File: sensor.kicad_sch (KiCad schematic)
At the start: 6 parts

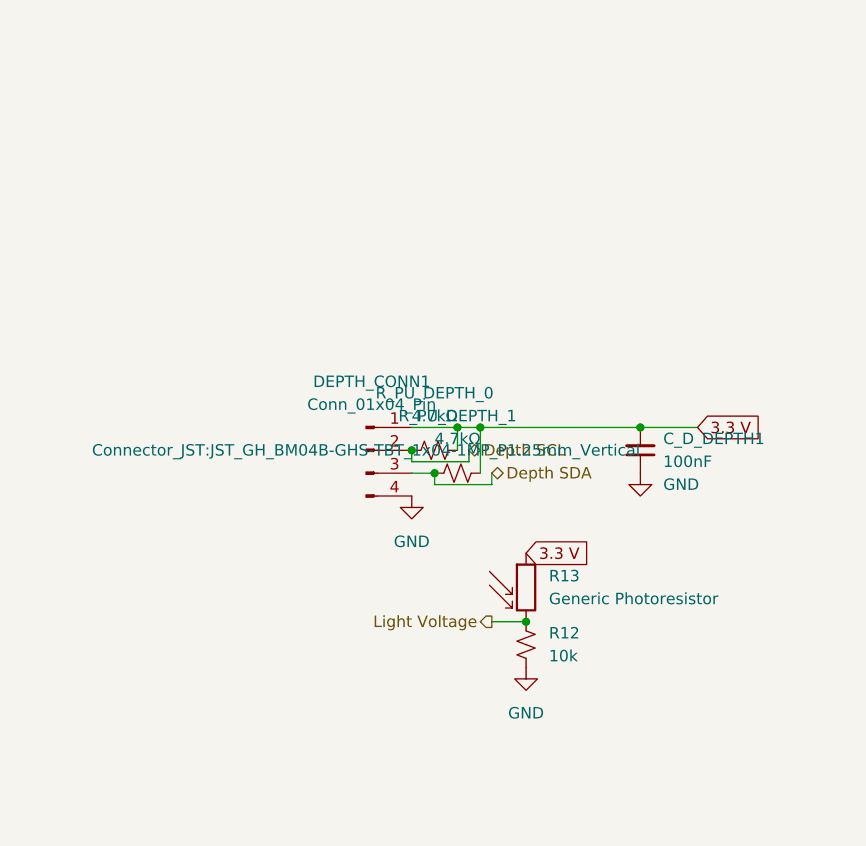
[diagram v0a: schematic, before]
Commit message: Updated Schematic
Updated schematic
Cleaned up dense portions
added H bridge
correct i2c wiring
added ferrite beads
added 12 V power monitoring
added stlink
added power mux
added power from usb
reformatted hierarichal sheets
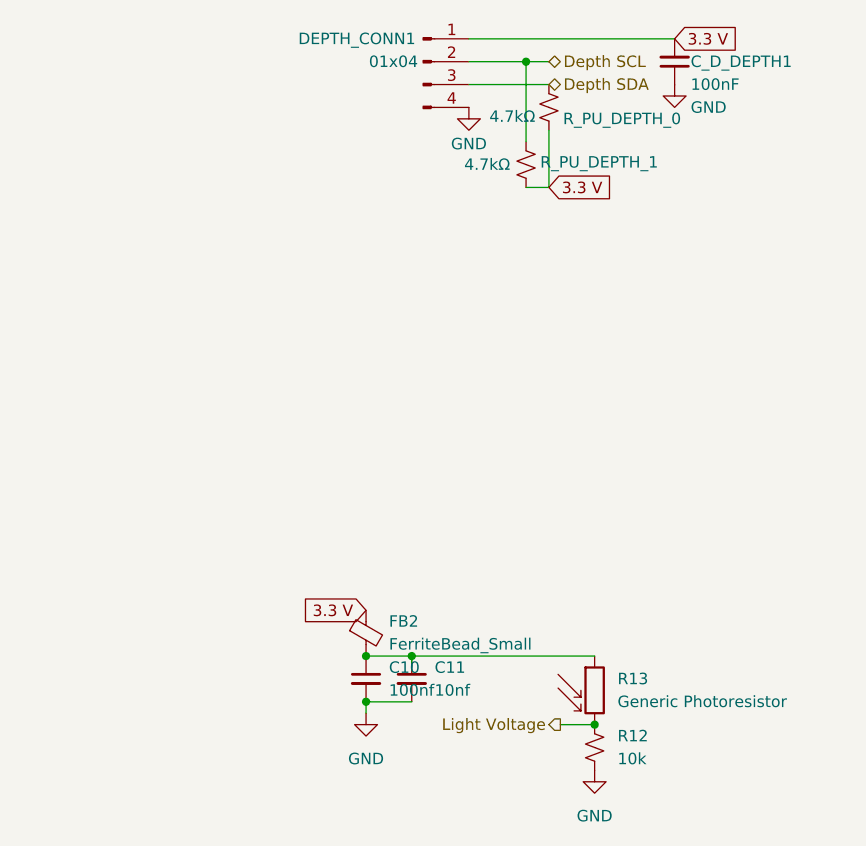
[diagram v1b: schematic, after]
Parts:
- added C10: 100nf, symbol Device:C_Small
- added C11: 10nf, symbol Device:C_Small
- added FB2: FerriteBead_Small, symbol Device:FerriteBead_Small
- DEPTH_CONN1: value Conn_01x04_Pin -> 01x04
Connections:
- net 3.3 V: now also R_PU_DEPTH_1.1, FB2.1; no longer R13.1, R_PU_DEPTH_1.2
- net Depth SCL: now also R_PU_DEPTH_1.2; no longer R_PU_DEPTH_0.1
- net Depth SDA: now also R_PU_DEPTH_0.1; no longer R_PU_DEPTH_1.1
- net GND: now also C10.2, C11.2
- new net: C10.1, C11.1, FB2.2, R13.1
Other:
- moved on the sheet: C_D_DEPTH1, DEPTH_CONN1, R12, R13, R_PU_DEPTH_0, R_PU_DEPTH_1

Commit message: USB, TVS, LDO, Passives, I2C
applied changes to usb circuitry, tvs, ldo, passibes and i2c.
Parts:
- removed R_PU_DEPTH_0, R_PU_DEPTH_1: 4.7kΩ, Resistor_SMD:R_0603_1608Metric, symbol Device:R_Small_US
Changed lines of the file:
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@@
-	)
-	(junction
-		(at 43.18 22.86)
-		(diameter 0)
-		(color 0 0 0 0)
 	)
 	(junction
@@
 	(wire
 		(pts
-			(xy 43.18 22.86) (xy 45.72 22.86)
+			(xy 36.83 22.86) (xy 45.72 22.86)
 		)
 		(stroke
@@
 	(wire
 		(pts
-			(xy 45.72 30.48) (xy 45.72 36.83)
+			(xy 50.8 88.9) (xy 30.48 88.9)
 		)
 		(stroke
@@
 	(wire
 		(pts
-			(xy 43.18 36.83) (xy 45.72 36.83)
+			(xy 36.83 25.4) (xy 45.72 25.4)
 		)
 		(stroke
@@
 	(wire
 		(pts
-			(xy 50.8 88.9) (xy 30.48 88.9)
+			(xy 25.4 93.98) (xy 25.4 95.25)
 		)
 		(stroke
@@
 	(wire
 		(pts
-			(xy 36.83 25.4) (xy 45.72 25.4)
-		)
-		(stroke
-			(width 0)
-			(type default)
-		)
-	)
-	(wire
-		(pts
-			(xy 25.4 93.98) (xy 25.4 95.25)
-		)
-		(stroke
-			(width 0)
-			(type default)
-		)
-	)
-	(wire
-		(pts
-			(xy 36.83 22.86) (xy 43.18 22.86)
-		)
-		(stroke
-			(width 0)
-			(type default)
-		)
-	)
-	(wire
-		(pts
 			(xy 25.4 93.98) (xy 30.48 93.98)
-		)
-		(stroke
-			(width 0)
-			(type default)
-		)
-	)
-	(wire
-		(pts
-			(xy 43.18 22.86) (xy 43.18 31.75)
 		)
 		(stroke
@@
 				)
 				(justify right)
-			)
-		)
-	)
-	(global_label "3.3 V"
-		(shape input)
-		(at 45.72 36.83 0)
-		(fields_autoplaced yes)
-		(effects
-			(font
-				(size 1.27 1.27)
-			)
-			(justify left)
-		)
-		(property "Intersheetrefs" "${INTERSHEET_REFS}"
-			(at 53.7852 36.83 0)
-			(hide yes)
-			(show_name no)
-			(do_not_autoplace no)
-			(effects
-				(font
-					(size 1.27 1.27)
-				)
-				(justify left)
 			)
 		)
@@
 	)
 	(symbol
-		(lib_id "Device:R_Small_US")
-		(at 43.18 34.29 180)
-		(unit 1)
-		(body_style 1)
-		(exclude_from_sim no)
-		(in_bom yes)
-		(on_board yes)
-		(in_pos_files yes)
-		(dnp no)
-		(property "Reference" "R_PU_DEPTH_1"
-			(at 51.308 34.036 0)
-			(show_name no)
-			(do_not_autoplace no)
-			(effects
-				(font
-					(size 1.27 1.27)
-				)
-			)
-		)
-		(property "Value" "4.7kΩ"
-			(at 38.862 34.29 0)
-			(show_name no)
-			(do_not_autoplace no)
-			(effects
-				(font
-					(size 1.27 1.27)
-				)
-			)
-		)
-		(property "Footprint" "Resistor_SMD:R_0603_1608Metric"
-			(at 43.18 34.29 0)
-			(hide yes)
-			(show_name no)
-			(do_not_autoplace no)
-			(effects
-				(font
-					(size 1.27 1.27)
-				)
-			)
-		)
-		(property "Datasheet" ""
-			(at 43.18 34.29 0)
-			(hide yes)
-			(show_name no)
-			(do_not_autoplace no)
-			(effects
-				(font
-					(size 1.27 1.27)
-				)
-			)
-		)
-		(property "Description" "Resistor, small US symbol"
-			(at 43.18 34.29 0)
-			(hide yes)
-			(show_name no)
-			(do_not_autoplace no)
-			(effects
-				(font
-					(size 1.27 1.27)
-				)
-			)
-		)
-		(pin "1"
-		)
-		(pin "2"
-		)
-		(instances
-			(project "X19-Float-Board"
-				(path "/00000000-0000-0000-0000-000060e6118b/5f356ab3-657b-42f3-9a8b-ebc79580ebf5"
-					(reference "R_PU_DEPTH_1")
-					(unit 1)
-				)
-			)
-		)
-	)
-	(symbol
 		(lib_id "Connector:Conn_01x04_Pin")
 		(at 31.75 22.86 0)
@@
 					(unit 1)
 				)
-			)
-		)
-	)
-	(symbol
-		(lib_id "Device:R_Small_US")
-		(at 45.72 27.94 0)
-		(unit 1)
-		(body_style 1)
-		(exclude_from_sim no)
-		(in_bom yes)
-		(on_board yes)
-		(in_pos_files yes)
-		(dnp no)
-		(property "Reference" "R_PU_DEPTH_0"
-			(at 53.848 29.21 0)
-			(show_name no)
-			(do_not_autoplace no)
-			(effects
-				(font
-					(size 1.27 1.27)
-				)
-			)
-		)
-		(property "Value" "4.7kΩ"
-			(at 41.656 28.956 0)
-			(show_name no)
-			(do_not_autoplace no)
-			(effects
-				(font
-					(size 1.27 1.27)
-				)
-			)
-		)
-		(property "Footprint" "Resistor_SMD:R_0603_1608Metric"
-			(at 45.72 27.94 0)
-			(hide yes)
-			(show_name no)
-			(do_not_autoplace no)
-			(effects
-				(font
-					(size 1.27 1.27)
-				)
-			)
-		)
-		(property "Datasheet" ""
-			(at 45.72 27.94 0)
-			(hide yes)
-			(show_name no)
-			(do_not_autoplace no)
-			(effects
-				(font
-					(size 1.27 1.27)
-				)
-			)
-		)
-		(property "Description" "Resistor, small US symbol"
-			(at 45.72 27.94 0)
-			(hide yes)
-			(show_name no)
-			(do_not_autoplace no)
-			(effects
-				(font
-					(size 1.27 1.27)
-				)
-			)
-		)
-		(pin "1"
-		)
-		(pin "2"
-		)
-		(instances
-			(project "X19-Float-Board"
-				(path "/00000000-0000-0000-0000-000060e6118b/5f356ab3-657b-42f3-9a8b-ebc79580ebf5"
-					(reference "R_PU_DEPTH_0")
-					(unit 1)
-				)

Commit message: footprints
footprints
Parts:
- removed FB2: FerriteBead_Small, symbol Device:FerriteBead_Small
- C10, C11: footprint (none) -> Capacitor_SMD:C_0603_1608Metric_Pad1.08x0.95mm_HandSolder
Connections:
- net 3.3 V: now also C10.1, C11.1, R13.1
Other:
- moved on the sheet: C10, C11
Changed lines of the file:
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@@
 	(paper "A4")
 	(junction
-		(at 25.4 88.9)
+		(at 30.48 85.09)
 		(diameter 0)
 		(color 0 0 0 0)
 	)
 	(junction
-		(at 30.48 88.9)
+		(at 25.4 85.09)
+		(diameter 0)
+		(color 0 0 0 0)
+	)
+	(junction
+		(at 50.8 96.52)
 		(diameter 0)
 		(color 0 0 0 0)
@@
 		(color 0 0 0 0)
 	)
-	(junction
-		(at 50.8 96.52)
-		(diameter 0)
-		(color 0 0 0 0)
-	)
 	(wire
 		(pts
@@
 	(wire
 		(pts
-			(xy 30.48 88.9) (xy 30.48 90.17)
-		)
-		(stroke
-			(width 0)
-			(type default)
-		)
-	)
-	(wire
-		(pts
-			(xy 25.4 88.9) (xy 30.48 88.9)
+			(xy 25.4 85.09) (xy 30.48 85.09)
 		)
 		(stroke
@@
 	(wire
 		(pts
-			(xy 50.8 88.9) (xy 30.48 88.9)
+			(xy 25.4 93.98) (xy 25.4 95.25)
+		)
+		(stroke
+			(width 0)
+			(type default)
+		)
+	)
+	(wire
+		(pts
+			(xy 50.8 85.09) (xy 30.48 85.09)
+		)
+		(stroke
+			(width 0)
+			(type default)
+		)
+	)
+	(wire
+		(pts
+			(xy 30.48 85.09) (xy 30.48 87.63)
 		)
 		(stroke
@@
 	(wire
 		(pts
-			(xy 25.4 93.98) (xy 25.4 95.25)
+			(xy 50.8 85.09) (xy 50.8 88.9)
+		)
+		(stroke
+			(width 0)
+			(type default)
+		)
+	)
+	(wire
+		(pts
+			(xy 30.48 93.98) (xy 30.48 92.71)
 		)
 		(stroke
@@
 		(pts
 			(xy 25.4 93.98) (xy 30.48 93.98)
+		)
+		(stroke
+			(width 0)
+			(type default)
+		)
+	)
+	(wire
+		(pts
+			(xy 25.4 74.93) (xy 25.4 85.09)
+		)
+		(stroke
+			(width 0)
+			(type default)
+		)
+	)
+	(wire
+		(pts
+			(xy 25.4 85.09) (xy 25.4 87.63)
+		)
+		(stroke
+			(width 0)
+			(type default)
+		)
+	)
+	(wire
+		(pts
+			(xy 25.4 93.98) (xy 25.4 92.71)
 		)
 		(stroke
@@
 	(global_label "3.3 V"
 		(shape input)
-		(at 25.4 83.82 180)
+		(at 25.4 74.93 180)
 		(fields_autoplaced yes)
 		(effects
@@
 		)
 		(property "Intersheetrefs" "${INTERSHEET_REFS}"
-			(at 17.3348 83.82 0)
+			(at 17.3348 74.93 0)
 			(hide yes)
 			(show_name no)
@@
 	(symbol
 		(lib_id "Device:C_Small")
-		(at 25.4 91.44 0)
+		(at 25.4 90.17 0)
+		(mirror y)
 		(unit 1)
 		(body_style 1)
@@
 		(in_pos_files yes)
 		(dnp no)
-		(fields_autoplaced yes)
 		(property "Reference" "C10"
-			(at 27.94 90.1762 0)
+			(at 22.86 88.9062 0)
 			(show_name no)
 			(do_not_autoplace no)
@@
 		)
 		(property "Value" "100nf"
-			(at 27.94 92.7162 0)
+			(at 22.86 91.4462 0)
 			(show_name no)
 			(do_not_autoplace no)
@@
 			)
 		)
-		(property "Footprint" ""
-			(at 25.4 91.44 0)
+		(property "Footprint" "Capacitor_SMD:C_0603_1608Metric_Pad1.08x0.95mm_HandSolder"
+			(at 25.4 90.17 0)
 			(hide yes)
 			(show_name no)
@@
 		)
 		(property "Datasheet" ""
-			(at 25.4 91.44 0)
+			(at 25.4 90.17 0)
 			(hide yes)
 			(show_name no)
@@
 		)
 		(property "Description" "Unpolarized capacitor, small symbol"
-			(at 25.4 91.44 0)
+			(at 25.4 90.17 0)
 			(hide yes)
 			(show_name no)
@@
 	)
 	(symbol
-		(lib_id "Device:FerriteBead_Small")
-		(at 25.4 86.36 0)
-		(unit 1)
-		(body_style 1)
-		(exclude_from_sim no)
-		(in_bom yes)
-		(on_board yes)
-		(in_pos_files yes)
-		(dnp no)
-		(fields_autoplaced yes)
-		(property "Reference" "FB2"
-			(at 27.94 85.0518 0)
-			(show_name no)
-			(do_not_autoplace no)
-			(effects
-				(font
-					(size 1.27 1.27)
-				)
-				(justify left)
-			)
-		)
-		(property "Value" "FerriteBead_Small"
-			(at 27.94 87.5918 0)
-			(show_name no)
-			(do_not_autoplace no)
-			(effects
-				(font
-					(size 1.27 1.27)
-				)
-				(justify left)
-			)
-		)
-		(property "Footprint" ""
-			(at 23.622 86.36 90)
-			(hide yes)
-			(show_name no)
-			(do_not_autoplace no)
-			(effects
-				(font
-					(size 1.27 1.27)
-				)
-			)
-		)
-		(property "Datasheet" ""
-			(at 25.4 86.36 0)
-			(hide yes)
-			(show_name no)
-			(do_not_autoplace no)
-			(effects
-				(font
-					(size 1.27 1.27)
-				)
-			)
-		)
-		(property "Description" "Ferrite bead, small symbol"
-			(at 25.4 86.36 0)
-			(hide yes)
-			(show_name no)
-			(do_not_autoplace no)
-			(effects
-				(font
-					(size 1.27 1.27)
-				)
-			)
-		)
-		(pin "1"
-		)
-		(pin "2"
-		)
-		(instances
-			(project "X19-Float-Board"
-				(path "/00000000-0000-0000-0000-000060e6118b/5f356ab3-657b-42f3-9a8b-ebc79580ebf5"
-					(reference "FB2")
-					(unit 1)
-				)
-			)
-		)
-	)
-	(symbol
 		(lib_id "Device:C_Small")
 		(at 59.69 22.86 180)
@@
 	(symbol
 		(lib_id "Device:C_Small")
-		(at 30.48 91.44 0)
+		(at 30.48 90.17 0)
 		(unit 1)
 		(body_style 1)
@@
 		(fields_autoplaced yes)
 		(property "Reference" "C11"
-			(at 33.02 90.1762 0)
+			(at 33.02 88.9062 0)
 			(show_name no)
 			(do_not_autoplace no)
@@
 		)
 		(property "Value" "10nf"
-			(at 33.02 92.7162 0)
+			(at 33.02 91.4462 0)
 			(show_name no)
 			(do_not_autoplace no)
@@
 			)
 		)
-		(property "Footprint" ""
-			(at 30.48 91.44 0)
+		(property "Footprint" "Capacitor_SMD:C_0603_1608Metric_Pad1.08x0.95mm_HandSolder"
+			(at 30.48 90.17 0)
 			(hide yes)
 			(show_name no)
@@
 		)
 		(property "Datasheet" ""
-			(at 30.48 91.44 0)
+			(at 30.48 90.17 0)
 			(hide yes)
 			(show_name no)
@@
 		)
 		(property "Description" "Unpolarized capacitor, small symbol"
-			(at 30.48 91.44 0)
-			(hide yes)
-			(show_name no)
+			(at 30.48 90.17 0)
+			(hide yes)
+			(show_name no)

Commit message: Finished footprints
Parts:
- R12: footprint (none) -> Capacitor_SMD:C_0603_1608Metric_Pad1.08x0.95mm_HandSolder
- R13: footprint (none) -> Resistor_SMD:R_1206_3216Metric_Pad1.30x1.75mm_HandSolder
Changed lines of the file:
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@@
 			)
 		)
-		(property "Footprint" ""
+		(property "Footprint" "Resistor_SMD:R_1206_3216Metric_Pad1.30x1.75mm_HandSolder"
 			(at 52.07 99.06 90)
 			(hide yes)
@@
 			)
 		)
-		(property "Footprint" ""
+		(property "Footprint" "Capacitor_SMD:C_0603_1608Metric_Pad1.08x0.95mm_HandSolder"
 			(at 50.8 99.06 0)
 			(hide yes)
